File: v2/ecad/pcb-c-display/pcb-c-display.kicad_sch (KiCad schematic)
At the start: 126 parts, among them Q1 AO3401A P-FET high side, Q2 2N7002, Q3 2N7002, Q4 2N7002, U1 PCA9555PW 0x22: LEDs + switch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, U2 PCA9555PW 0x23: LEDs, bar, e-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, U5 USBLC6-2SC6 (2-line TVS), U6 USBLC6-2SC6 (2-line TVS), U7 USBLC6-2SC6 (2-line TVS), U8 USBLC6-2SC6 (2-line TVS)

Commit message: feat(release): A18 (dock holes 1.1 mm for the Preci-Dip 813 connector) and E3 (junction D-hole flat per the Amphenol 132170 drawing), C4 schematic with the switch part numbers, handoff rebuilt, A17 and E2 retired [MESHSAT-709]
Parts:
- SW_EMCON: value EMCON guarded latching toggle (closed = TX inhibit) -> EMCON guarded latching toggle (closed = TX inhibit); NKK M2012SD3A01, guard per ASSEMBLY.md section 9
- SW_LIGHT: value LIGHTING DAY/NIGHT/BLACKOUT toggle DPDT ON-ON-ON (pole 1: rail, pole 2: sense) -> LIGHTING DAY/NIGHT/BLACKOUT toggle DPDT ON-ON-ON (pole 1: rail, pole 2: sense); NKK M2044SD3A01 + AT401A boot
- SW_MAIN: value MAIN PWR 19 mm momentary, green ring (to X1202 external switch) -> MAIN PWR 19 mm momentary, green ring (to X1202 external switch); C&K ATP19-SL1-603-B0SA-03G
- SW_PI: value PI 16 mm recessed momentary, amber ring (to Pi 5 J2) -> PI 16 mm recessed momentary, amber ring (to Pi 5 J2); C&K ATP16-SL1-403-M0SA-04G (orange ring)
- SW_SOS: value SOS guarded momentary toggle (red cover) -> SOS guarded momentary toggle (red cover); NKK M2015SD3A01, guard per ASSEMBLY.md section 9
- SW_TEST: value TEST/ACK 16 mm momentary, white ring -> TEST/ACK 16 mm momentary, white ring; C&K ATP16-SL1-203-M0SA-04G
- SW_ZERO: value ZEROIZE guarded momentary toggle (hold 5 s) -> ZEROIZE guarded momentary toggle (hold 5 s); NKK M2015SD3A01, guard per ASSEMBLY.md section 9

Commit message: feat(ecad): PCB-C C5 finished, the sealed face (0 hard, 0 unrouted, 272 vias); die-cut seal outlines as DXF; case template with the seal parts named [MESHSAT-709]
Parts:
- removed J_X1202SW: lead to the X1202 external-switch pins (XH2.5), Connector_JST:JST_XH_B2B-XH-A_1x02_P2.50mm_Vertical, symbol Connector_Generic:Conn_01x02
- added J_MAINSW: MAIN button lead to PCB-A J_MAINSW (XH2.5 at the 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, meshsat:LeadLands_1x02, symbol Connector_Generic:Conn_01x02
- BZ1: value active piezo 5 V 85 dB -> IP67 panel-mount sounder, 5 V DC continuous, bezel gasket on the face, two flying leads (part per docs/respin-research-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; footprint Buzzer_Beeper:Buzzer_12x9.5RM7.6 -> meshsat:PanelSounder
- H1, H10, H11, H12, H13, H14, H15, H16, H2, H3, H4, H5, H6, H7, H8, H9: value frame screw M3, GND bond -> frame screw M3 x 10, GND bond through the bonded sealing washer on the underside land; footprint MountingHole:MountingHole_3.2mm_M3_Pad -> meshsat:FrameScrew_M3_GND
- J_EPD: value e-paper module lead: BUSY RES D/C CS SCL SDA GND VCC -> e-paper module lead: BUSY RES D/C CS SCL SDA GND VCC (SMD header on the underside); footprint Connector_PinHeader_2.54mm:PinHeader_1x08_P2.54mm_Vertical -> Connector_PinHeader_2.54mm:PinHeader_1x08_P2.54mm_Vertical_SMD_Pin1Left
- J_PANEL: footprint Connector_IDC:IDC-Header_2x10_P2.54mm_Vertical -> Connector_IDC:IDC-Header_2x10_P2.54mm_Vertical_SMD
- J_PIJ2: value lead to the Pi 5 J2 power-button pads (XH2.5) -> lead to the Pi 5 J2 power-button pins: two solder lands on the underside, soldered and beaded; footprint Connector_JST:JST_XH_B2B-XH-A_1x02_P2.50mm_Vertical -> meshsat:LeadLands_1x02
- SW_EMCON: value EMCON guarded latching toggle (closed = TX inhibit); NKK M2012SD3A01, guard per ASSEMBLY.md section 9 -> EMCON locking toggle (closed = TX inhibit; APEM 5636ADKB-2V, both positions locked; ruling 32.13); K front seal in the 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
- SW_LIGHT: value LIGHTING DAY/NIGHT/BLACKOUT toggle DPDT ON-ON-ON (pole 1: rail, pole 2: sense); NKK M2044SD3A01 + AT401A boot -> LIGHTING DAY/NIGHT/BLACKOUT toggle DPDT ON-ON-ON (pole 1: rail, pole 2: sense); NKK M2044SD3A01 on the D3 splashproof b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
- SW_MAIN: value MAIN PWR 19 mm momentary, green ring (to X1202 external switch); C&K ATP19-SL1-603-B0SA-03G -> MAIN PWR 19 mm momentary, green ring (to PCB-A J_MAINSW); C&K ATP19-SL1-603-B0SA-03G; silicone gasket washer under the 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
- SW_PI: value PI 16 mm recessed momentary, amber ring (to Pi 5 J2); C&K ATP16-SL1-403-M0SA-04G (orange ring) -> PI 16 mm recessed momentary, amber ring (to Pi 5 J2); C&K ATP16-SL1-403-M0SA-04G (orange ring); silicone gasket washer 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
- SW_SOS: value SOS guarded momentary toggle (red cover); NKK M2015SD3A01, guard per ASSEMBLY.md section 9 -> SOS locking toggle, maintained (APEM 5636ADKB-2V, both positions locked, red boot; ruling 32.13); K front seal in the k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
- SW_TEST: value TEST/ACK 16 mm momentary, white ring; C&K ATP16-SL1-203-M0SA-04G -> TEST/ACK 16 mm momentary, white ring; C&K ATP16-SL1-203-M0SA-04G; silicone gasket washer under the bezel
- SW_ZERO: value ZEROIZE guarded momentary toggle (hold 5 s); NKK M2015SD3A01, guard per ASSEMBLY.md section 9 -> ZEROIZE locking toggle, maintained (APEM 5636ADKB-2V, both positions locked; ruling 32.13); K front seal in the keyed 6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
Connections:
- net X1202SW_A renamed MAINSW_A
- net X1202SW_A2 renamed MAINSW_A2
- net MAINSW_A2: now also J_MAINSW.1 (Pin_1)
- net X1202SW_B renamed MAINSW_B
- net X1202SW_B2 renamed MAINSW_B2
- net MAINSW_B2: now also J_MAINSW.2 (Pin_2)

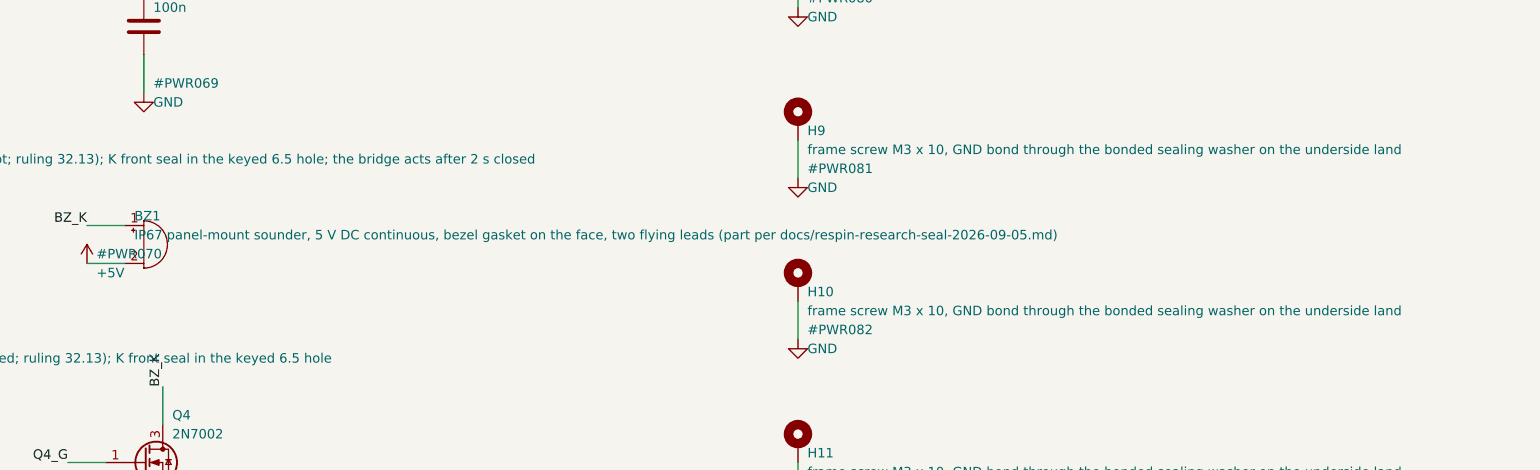
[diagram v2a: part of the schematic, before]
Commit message: docs: date correction, every event of section 32.10 onward is 4 September 2026 (headers carry the commit clock, research notes renamed); superseded board folders moved under boards/superseded [MESHSAT-709]
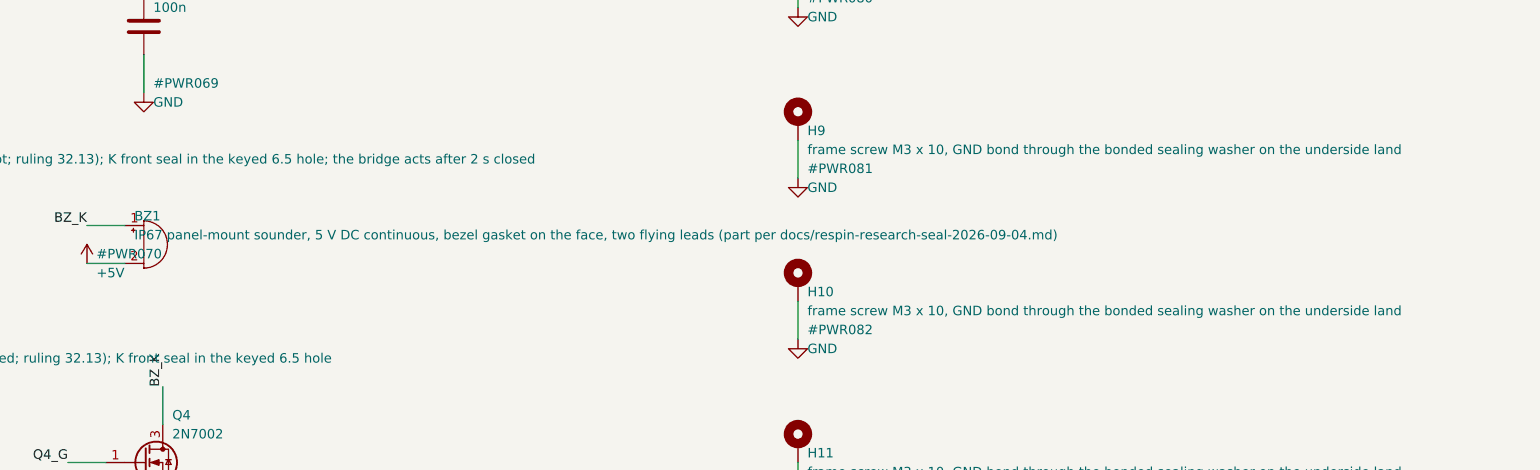
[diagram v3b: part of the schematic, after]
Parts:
- BZ1: value IP67 panel-mount sounder, 5 V DC continuous, bezel gasket on the face, two flying leads (part per docs/respin-research-seal-2026-09-05.md) -> IP67 panel-mount sounder, 5 V DC continuous, bezel gasket on the face, two flying leads (part per docs/respin-research-seal-2026-09-04.md)
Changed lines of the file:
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@@
 	(generator_version "9.0")
 	(paper "A1")
-	(title_block (title "MeshSat Field Kit carrier - PCB-C CONTROL PANEL") (date "2026-09-05") (rev "A") (company "MeshSat") (comment 1 "Phase C5 schematic (sealed face: no through-hole connector, panel-mount sounder, masked frame rings), generated by tools/gen_sch_c.py. Netlist style: every pin carries a stub and a net label.") (comment 2 "MESHSAT-709. FE1.1s hub on internal regulators; TPS2065C x2 + TPS22810 x4 switches (B4: LoRa and RockBLOCK channels at 2 A for the T-Beam 1W and 9704 bursts); INA219 per channel; PCA9555 EN/FAULT; both Pi UARTs to the RockBLOCK site via JP3/JP4."))
+	(title_block (title "MeshSat Field Kit carrier - PCB-C CONTROL PANEL") (date "2026-09-04") (rev "A") (company "MeshSat") (comment 1 "Phase C5 schematic (sealed face: no through-hole connector, panel-mount sounder, masked frame rings), generated by tools/gen_sch_c.py. Netlist style: every pin carries a stub and a net label.") (comment 2 "MESHSAT-709. FE1.1s hub on internal regulators; TPS2065C x2 + TPS22810 x4 switches (B4: LoRa and RockBLOCK channels at 2 A for the T-Beam 1W and 9704 bursts); INA219 per channel; PCA9555 EN/FAULT; both Pi UARTs to the RockBLOCK site via JP3/JP4."))
 	(text "RIBBON FROM PCB-B, RAILS, TVS, TEST POINTS" (exclude_from_sim no) (at 5.08 25.40 0) (effects (font (size 2.00 2.00) bold) (justify left bottom)))
 	(symbol (lib_id "Connector_Generic:Conn_02x10_Odd_Even") (at 39.37 53.34 0) (unit 1) (exclude_from_sim no) (in_bom yes) (on_board yes) (dnp no) (fields_autoplaced yes)
@@
 	(symbol (lib_id "Device:Buzzer") (at 656.59 234.95 0) (unit 1) (exclude_from_sim no) (in_bom yes) (on_board yes) (dnp no) (fields_autoplaced yes)
 		(property "Reference" "BZ1" (at 655.32 231.14 0) (effects (font (size 1.27 1.27)) (justify left)))
-		(property "Value" "IP67 panel-mount sounder, 5 V DC continuous, bezel gasket on the face, two flying leads (part per docs/respin-research-seal-2026-09-05.md)" (at 655.32 233.68 0) (effects (font (size 1.27 1.27)) (justify left)))
+		(property "Value" "IP67 panel-mount sounder, 5 V DC continuous, bezel gasket on the face, two flying leads (part per docs/respin-research-seal-2026-09-04.md)" (at 655.32 233.68 0) (effects (font (size 1.27 1.27)) (justify left)))
 		(property "Footprint" "meshsat:PanelSounder" (at 656.59 234.95 0) (effects (font (size 1.27 1.27)) (justify left) (hide yes)))
 		(property "Datasheet" "" (at 656.59 234.95 0) (effects (font (size 1.27 1.27)) (justify left) (hide yes)))

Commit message: feat(pcb-c): C6, the four-layer backer routed clean (0 hard, 0 open, 240 router vias); deliverable meshsat-pcb-c-revA-C6; order and review sets rebuilt with B15 and C6, B14 and C5 under superseded [MESHSAT-813]
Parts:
- removed H10, H11, H12, H13, H14, H15, H16, H7, H8, H9: frame screw M3 x 10, GND bond through the bonded 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, meshsat:FrameScrew_M3_GND, symbol Mechanical:MountingHole_Pad
- H1, H2, H3, H4, H5, H6: value frame screw M3 x 10, GND bond through the bonded sealing washer on the underside land -> M3 x 6 into the face plate's self-clinching standoff (C6 backer, 5 Sep 2026): GND bond to the plate; footprint meshsat:FrameScrew_M3_GND -> meshsat:BackerScrew_M3_GND
- SW_EMCON, SW_SOS, SW_ZERO: footprint meshsat:GuardedToggle_SPDT -> meshsat:ToggleBody_SPDT
- SW_LIGHT: footprint meshsat:PanelToggle_DPDT -> meshsat:ToggleBody_DPDT
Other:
- note added: "PLATE STANDOFF SCREWS, GND BOND"
- note removed: "FRAME SCREWS, GND BOND"

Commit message: feat(release): C7 (the panel backer ring) routed clean on the box, deliverable meshsat-pcb-c-revA-C7 [MESHSAT-830]
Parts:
- removed J_EPD: e-paper module lead: BUSY RES D/C CS SCL SDA GND 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, Connector_PinHeader_2.54mm:PinHeader_1x08_P2.54mm_Vertical_SMD_Pin1Left, symbol Connector_Generic:Conn_01x08
- removed J_PANEL: panel ribbon from PCB-B (IDC 2x10, underside), Connector_IDC:IDC-Header_2x10_P2.54mm_Vertical_SMD, symbol Connector_Generic:Conn_02x10_Odd_Even
- removed U5: USBLC6-2SC6 (2-line TVS), Package_TO_SOT_SMD:SOT-23-6, symbol Power_Protection:USBLC6-2SC6
- added C14, C15, C16: 1u, Capacitor_SMD:C_0603_1608Metric, symbol Device:C
- added C17, C18, C25, C26, C27, C29, C38: 100n, Capacitor_SMD:C_0603_1608Metric, symbol Device:C
- added C19, C20, C21, C22, C23, C24: 10n, Capacitor_SMD:C_0603_1608Metric, symbol Device:C
- added C28: 4.7u, Capacitor_SMD:C_0805_2012Metric, symbol Device:C
- added C30, C31, C32, C33, C34, C35, C36, C37: 1u 25V, Capacitor_SMD:C_0603_1608Metric, symbol Device:C
- added CAM_H1, CAM_H2: M2 screw of the USB camera module (25 x 25 board,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, MountingHole:MountingHole_2.2mm_M2, symbol Mechanical:MountingHole
- added D18: status (GPIO25), LED_SMD:LED_0603_1608Metric, symbol Device:LED
- added D19: SS2040FL: EPD_SW -> VGH, Diode_SMD:D_SOD-123F, symbol Device:D_Schottky
- added D20: SS2040FL: pump clamp, Diode_SMD:D_SOD-123F, symbol Device:D_Schottky
- added D21: SS2040FL: pump -> VGL, Diode_SMD:D_SOD-123F, symbol Device:D_Schottky
- added H7, H8: M3 x 6 into the face plate's self-clinching stand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, meshsat:BackerScrew_M3_GND, symbol Mechanical:MountingHole_Pad
- added J_EPD: Hirose FH34SRJ-24S-0.5SH ZIF for the E2370KS0C1 f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, meshsat:Hirose_FH34SRJ-24S, symbol Connector_Generic:EPD24
- added J_HSJ1: U-174/U headset jack 1 (Amphenol Nexus class, dra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, meshsat:PanelJack_17mm, symbol Mechanical:MountingHole
- added J_HSJ2: U-174/U headset jack 2 (Amphenol Nexus class, dra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, meshsat:PanelJack_17mm, symbol Mechanical:MountingHole
- added J_PANEL: panel ribbon from B16 J_PANEL (IDC 2x13 SMD, unde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, Connector_IDC:IDC-Header_2x13_P2.54mm_Vertical_SMD, symbol Connector_Generic:Conn_02x13_Odd_Even
- added L1: 10uH ATNR4010100MT 0.8 A (the boost inductor), Inductor_SMD:L_APV_ANR4020, symbol Device:L
- added Q5: AO3401A P-FET: the e-paper's supply switch (EPD_P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, Package_TO_SOT_SMD:SOT-23, symbol Transistor_FET:AO3401A
- added Q6: Si1308EDL class N-FET (RDS under 200 mOhm, VGS 2.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, Package_TO_SOT_SMD:SOT-23, symbol Transistor_FET:2N7002
- added R40: 300R, Resistor_SMD:R_0603_1608Metric, symbol Device:R
- added R41: 470R, Resistor_SMD:R_0603_1608Metric, symbol Device:R
- added R42: 10k, Resistor_SMD:R_0603_1608Metric, symbol Device:R
- added R43: 0.47R 1%, Resistor_SMD:R_0603_1608Metric, symbol Device:R
- added R44: 100R, Resistor_SMD:R_0603_1608Metric, symbol Device:R
- added R45: 100k, Resistor_SMD:R_0603_1608Metric, symbol Device:R
- added TP14: SPARE2, TestPoint:TestPoint_Pad_D1.5mm, symbol Connector:TestPoint
- added TP15: SPARE3, TestPoint:TestPoint_Pad_D1.5mm, symbol Connector:TestPoint
- added TP16: SPARE4, TestPoint:TestPoint_Pad_D1.5mm, symbol Connector:TestPoint
- added TP17: SPARE5, TestPoint:TestPoint_Pad_D1.5mm, symbol Connector:TestPoint
- added TP18: SPARE6, TestPoint:TestPoint_Pad_D1.5mm, symbol Connector:TestPoint
- added TP19: SPARE7, TestPoint:TestPoint_Pad_D1.5mm, symbol Connector:TestPoint
- added TP20: SPARE8, TestPoint:TestPoint_Pad_D1.5mm, symbol Connector:TestPoint
- added TP21: SPARE9, TestPoint:TestPoint_Pad_D1.5mm, symbol Connector:TestPoint
- added TP22: SPARE10, TestPoint:TestPoint_Pad_D1.5mm, symbol Connector:TestPoint
- added TP23: SPARE11, TestPoint:TestPoint_Pad_D1.5mm, symbol Connector:TestPoint
- added TP24: SPARE12, TestPoint:TestPoint_Pad_D1.5mm, symbol Connector:TestPoint
- added TP25: EPD_BUSY, TestPoint:TestPoint_Pad_D1.5mm, symbol Connector:TestPoint
- added TP26: EPD_VGH, TestPoint:TestPoint_Pad_D1.5mm, symbol Connector:TestPoint
- added TP27: EPD_VGL, TestPoint:TestPoint_Pad_D1.5mm, symbol Connector:TestPoint
- added TP28: HB1, TestPoint:TestPoint_Pad_D1.5mm, symbol Connector:TestPoint
- added TP29: HB2, TestPoint:TestPoint_Pad_D1.5mm, symbol Connector:TestPoint
- added TP30: HB3, TestPoint:TestPoint_Pad_D1.5mm, symbol Connector:TestPoint
- added TP31: SLOT_EN1, TestPoint:TestPoint_Pad_D1.5mm, symbol Connector:TestPoint
- added TP32: SLOT_EN2, TestPoint:TestPoint_Pad_D1.5mm, symbol Connector:TestPoint
- added TP33: SLOT_EN3, TestPoint:TestPoint_Pad_D1.5mm, symbol Connector:TestPoint
- added TP34: HDMI_SEL1, TestPoint:TestPoint_Pad_D1.5mm, symbol Connector:TestPoint
- added TP35: HDMI_SEL2, TestPoint:TestPoint_Pad_D1.5mm, symbol Connector:TestPoint
- added TP36: PI_SHDN_REQ, TestPoint:TestPoint_Pad_D1.5mm, symbol Connector:TestPoint
- added TP37: PI_KILL, TestPoint:TestPoint_Pad_D1.5mm, symbol Connector:TestPoint
- added TP38: SHORE_INHIBIT, TestPoint:TestPoint_Pad_D1.5mm, symbol Connector:TestPoint
- added TP39: PIJ2_A, TestPoint:TestPoint_Pad_D1.5mm, symbol Connector:TestPoint
- added TP40: PIJ2_B, TestPoint:TestPoint_Pad_D1.5mm, symbol Connector:TestPoint
- added U3: RP2040 panel controller (USB device on B16's slot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, Package_DFN_QFN:QFN-56-1EP_7x7mm_P0.4mm_EP3.2x3.2mm, symbol Connector_Generic:RP2040
- added U4: W25Q16JVUXIQ 16 Mbit QSPI flash (USON-8: 1 CS 2 D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, Package_SON:Winbond_USON-8-1EP_3x2mm_P0.5mm_EP0.2x1.6mm, symbol Connector_Generic:Conn_01x09
- added U5: TLV75533PDBV 3.3 V 500 mA LDO for the controller,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, Package_TO_SOT_SMD:SOT-23-5, symbol Connector_Generic:Conn_01x05
- added U9: 74LVC1G04 inverter (2 A 4 Y): EMCON_HW = NOT TX_I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, Package_TO_SOT_SMD:SOT-23-5, symbol Connector_Generic:Conn_01x05
- added U_LIGHT: Vishay VEML7700 ambient light sensor (1 SCL 2 VDD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, meshsat:Vishay_VEML7700, symbol Connector_Generic:Conn_01x04
- added Y1: 12 MHz ABM8-272-T3 (3225): 1 XIN, 3 XOUT, 2 and 4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, Crystal:Crystal_SMD_3225-4Pin_3.2x2.5mm, symbol Device:Crystal_GND24
- BZ1: value IP67 panel-mount sounder, 5 V DC continuous, bezel gasket on the face, two flying leads (part per docs/respin-research-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 -> IP67 panel-mount sounder, 5 V DC continuous, bezel gasket on the face, two flying leads (Floyd Bell MC-09-530-Q class)
- C10, C7, C8, C9: value 10n -> 100n; LCSC C57112 -> (none)
- C11, C12, C13: LCSC C14663 -> (none)
- C3, C4: value 100n -> 1u; LCSC C14663 -> (none)
- C5, C6: value 10n -> 15p NP0; footprint Capacitor_SMD:C_0603_1608Metric -> Capacitor_SMD:C_0402_1005Metric; LCSC C57112 -> (none)
- H1, H2, H3, H4, H5, H6: value M3 x 6 into the face plate's self-clinching standoff (C6 backer, 5 Sep 2026): GND bond to the plate -> M3 x 6 into the face plate's self-clinching standoff: GND bond to the plate
- JP1: value PANEL_ID strap (closed = variant B) -> BOOTSEL: short while powering to enter the USB bootloader
- JP2: value EPD RES from BCM7 instead of U2 (close to use) -> PANEL_ID strap (closed = variant B)
- J_MAINSW: value MAIN button lead to PCB-A J_MAINSW (XH2.5 at the PCB-A end): two solder lands on the underside, soldered and beaded -> MAIN button lead to A22 J_MAINSW (XH2.5 at the A22 end): two solder lands on the underside, soldered and beaded
- J_PIJ2: value lead to the Pi 5 J2 power-button pins: two solder lands on the underside, soldered and beaded -> PI button lead: two solder lands on the underside (the controller reads it as the module shutdown request)
- R1: value 10k -> 1k; LCSC C25804 -> (none)
- R10: value 47R -> 10k; LCSC C25118 -> C25804
- R11: value 100R -> 10k; LCSC C22775 -> C25804
- R12: value 100k -> 10k; LCSC C25803 -> C25804
- R13, R15: value 300R -> 10k; LCSC C23025 -> C25804
- R14: value 300R -> 100k; LCSC C23025 -> C25803
- R16: value 180R -> 10k; LCSC C25270 -> C25804
- R17: value 180R -> 2.2k; LCSC C25270 -> C4190
- R18: value 180R -> 47R; LCSC C25270 -> C25118
- R19: value 180R -> 100R; LCSC C25270 -> C22775
- R2, R3: value 10k -> 27R; LCSC C25804 -> (none)
- R20: value 180R -> 100k; LCSC C25270 -> C25803
- R21, R22: value 180R -> 300R; LCSC C25270 -> C23025
- R28, R32: value 300R -> 180R; LCSC C23025 -> C25270
- R29: value 1k -> 180R; LCSC C11702 -> C25270
- R30: value 100k -> 180R; LCSC C25803 -> C25270
- R31: value 470R -> 300R; LCSC C23179 -> C23025
- R33: value 470R -> 180R; LCSC C23179 -> C25270
- R34, R35: value 100R -> 180R; LCSC C22775 -> C25270
- R36: value 100R -> 300R; LCSC C22775 -> C23025
- R37: value 100R -> 1k; LCSC C22775 -> C11702
- R38: value 100R -> 100k; LCSC C22775 -> C25803
- R39: value 100k -> 470R; LCSC C25803 -> C23179
- R4: LCSC C25804 -> (none)
- R5: value 10k -> 1k (BOOTSEL); LCSC C25804 -> (none)
- R6: value 100k -> 1k; LCSC C25803 -> (none)
- R7, R8: value 10k -> 2.2k; LCSC C25804 -> (none)
- R9: value 2.2k -> 10k; LCSC C4190 -> C25804
- SW_EMCON: value EMCON locking toggle (closed = TX inhibit; APEM 5636ADKB-2V, both positions locked; ruling 32.13); K front seal in the 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 -> EMCON locking toggle (closed = TX inhibit, a hardware line: TX_INHIBIT_n low and EMCON_HW high; APEM 5636ADKB-2V, hinge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
- SW_MAIN: value MAIN PWR 19 mm momentary, green ring (to PCB-A J_MAINSW); C&K ATP19-SL1-603-B0SA-03G; silicone gasket washer under the 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 -> MAIN PWR 19 mm momentary, green ring (to A22 J_MAINSW); C&K ATP19-SL1-603-B0SA-03G; silicone gasket washer under the be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
- SW_PI: value PI 16 mm recessed momentary, amber ring (to Pi 5 J2); C&K ATP16-SL1-403-M0SA-04G (orange ring); silicone gasket washer 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 -> PI 16 mm recessed momentary, amber ring (PI_SHDN_REQ to the modules through the controller); C&K ATP16-SL1-403-M0SA-04G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
- SW_SOS: value SOS locking toggle, maintained (APEM 5636ADKB-2V, both positions locked, red boot; ruling 32.13); K front seal in the k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 -> SOS locking toggle, maintained (APEM 5636ADKB-2V, both positions locked, red boot, hinged safety cover per 32.50; rulin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
- SW_ZERO: value ZEROIZE locking toggle, maintained (APEM 5636ADKB-2V, both positions locked; ruling 32.13); K front seal in the keyed 6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 -> ZEROIZE locking toggle, maintained (APEM 5636ADKB-2V, hinged safety cover; ruling 32.13); K front seal in the keyed 6.5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
- TP1: value LED_RAIL -> SWCLK
- TP10: value SPARE3 -> TX_INHIBIT_n
- TP11: value SPARE4 -> EMCON_HW
- TP12: value SPARE5 -> ZEROIZE_HW
- TP13: value EPD_BUSY -> SPARE1
- TP2: value LED_RAIL_SW -> SWDIO
- TP3: value +5V -> C_RUN
- TP4: value +3V3 -> LED_RAIL
- TP5: value GND -> LED_RAIL_SW
- TP6: value EXP_INT -> +5V
- TP7: value TX_INHIBIT_n -> +3V3
- TP8: value SPARE1 -> GND
- TP9: value SPARE2 -> EXP_INT
- U1: value PCA9555PW 0x22: LEDs + switches -> PCA9555PW 0x22: LED sinks, light mode inputs
- U2: value PCA9555PW 0x23: LEDs, bar, e-paper control -> PCA9555PW 0x23: LED sinks, the battery bar, lamp test
- U6, U7, U8: value USBLC6-2SC6 (2-line TVS) -> USBLC6-2SC6
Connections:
- net EPD_CS_F is gone; now on net TX_A: R36.2
- net EPD_DC_F is gone; now on net Q3_G: R37.2
- net EPD_RES_ALT is gone; now on net PANEL_ID: JP2.1 (A)
- net EPD_SCL_F is gone; now on net BAT4_A: R34.2
- net EPD_SDA_F is gone; now on net BAT5_A: R35.2
- net SPI_MOSI is gone; now on net LED_RAIL: R35.1
- net SPI_SCLK is gone; now on net LED_RAIL: R34.1
- net +3V3: now also C10.1, C11.1, C12.1, C7.1, C8.1, C9.1, R10.2, R11.2, R12.2, R13.2, R14.2, R16.2, R7.2, R9.2, TP7.1, C16.1, C17.1, C18.1, C25.1, C38.1, Q5.2 (S), R42.2, U3.1 (IOVDD), U3.10 (IOVDD), U3.22 (IOVDD), U3.33 (IOVDD), U3.42 (IOVDD), U3.43 (ADC_AVDD), U3.44 (VREG_VIN), U3.48 (USB_VDD), U3.49 (IOVDD), U4.8 (Pin_8), U5.5 (Pin_5), U9.5 (Pin_5), U_LIGHT.2 (Pin_2); no longer C3.1, R1.2, R2.2, R3.2, R5.2, R6.2, TP4.1
- net +5V: now also C3.1, TP6.1, J_PANEL.1 (Pin_1), J_PANEL.2 (Pin_2), U5.1 (Pin_1), U5.3 (Pin_3); no longer TP3.1
- net BAT1_A: now also R31.2; no longer R23.2
- net BAT2_A: now also R32.2; no longer R24.2
- net BAT3_A: now also R33.2; no longer R25.2
- net BAT4_A: no longer R26.2
- net BAT5_A: no longer R27.2
- net CHG_A: now also R29.2; no longer R21.2
- net EPD_BUSY: now also J_EPD.9 (BUSY_N), TP25.1, U3.9 (GPIO7); no longer TP13.1, U2.15 (IO1_2)
- net EPD_DC: now also J_EPD.11 (DC), U3.6 (GPIO4); no longer R37.1, U6.3 (I/O2), U6.4 (I/O2)
- net EXP_INT: now also TP9.1, U8.3 (I/O2), U8.4 (I/O2), J_PANEL.6 (Pin_6), U3.36 (GPIO24); no longer TP6.1
- net GND: now also C11.2, C12.2, JP2.2 (B), R20.2, R38.2, TP8.1, C14.2, C15.2, C16.2, C17.2, C18.2, C19.2, C20.2, C21.2, C22.2, C23.2, C24.2, C25.2, C28.2, C29.2, C30.2, C32.2, C33.2, C34.2, C35.2, C36.2, C37.2, C38.2, D18.1 (K), D20.2 (A), H7.1, H8.1, J_EPD.17 (VSS), J_EPD.25 (SHIELD), J_EPD.26 (SHIELD), J_EPD.8 (BS), J_PANEL.14 (Pin_14), J_PANEL.17 (Pin_17), J_PANEL.3 (Pin_3), J_PANEL.9 (Pin_9), R43.2, R45.2, U3.19 (TESTEN), U3.57 (GND), U4.4 (Pin_4), U4.9 (Pin_9), U5.2 (Pin_2), U9.3 (Pin_3), U_LIGHT.3 (Pin_3), Y1.2 (G), Y1.4 (G); no longer R12.2, R30.2, R39.2, TP5.1
- net GPS_A: now also R27.2; no longer R19.2
- net LED_RAIL: now also R29.1, R30.1, R31.1, R36.1, TP4.1, R40.1, R41.1; no longer R13.1, R14.1, R15.1, R16.1, R17.1, R18.1, R19.1, R20.1, TP1.1
- net LED_RAIL_SW: now also R15.1, R17.1, R39.1, TP5.1; no longer R31.1, R7.1, R9.1, TP2.1
- net LIGHT_DAY_n: now also R12.1, U1.13 (IO1_0), C22.1; no longer C8.1, R4.1, U1.17 (IO1_4)
- net LIGHT_NIGHT_n: now also R13.1, U1.14 (IO1_1), C23.1; no longer C9.1, R5.1, U1.18 (IO1_5)
- net LTE_A: now also R26.2; no longer R18.2
- net MAINRING_A: now also R39.2; no longer R31.2
- net MAINSW_A2: now also C26.1; no longer C11.1
- net MAINSW_B2: now also C26.2; no longer C11.2
- net MCAUT_A: now also R22.2; no longer R14.2
- net MESH_A: now also R25.2; no longer R17.2
- net MSG_A: now also R30.2; no longer R22.2
- net MWARN_A: now also R21.2; no longer R13.2
- net PANEL_ID: now also R16.1, U1.15 (IO1_2); no longer JP1.1 (A), R8.1, U1.20 (IO1_7)
- net PANEL_PWM: now also R19.1, U3.11 (GPIO8); no longer R11.1, U8.1 (I/O1), U8.6 (I/O1)
- net PIJ2_A: now also TP39.1
- net PIJ2_A2: now also C27.1; no longer C12.1
- net PIJ2_B: now also TP40.1
- net PIJ2_B2: now also C27.2; no longer C12.2
- net PIRING_A: now also R40.2; no longer R32.2
- net PWM1: now also R44.1, U3.12 (GPIO9); no longer R38.1, U8.3 (I/O2), U8.4 (I/O2)
- net Q1_G: now also R17.2, R18.1; no longer R10.1, R9.2
- net Q2_D: now also R18.2; no longer R10.2
- net Q2_G: now also R19.2, R20.1; no longer R11.2, R12.1
- net Q3_G: now also R38.1; no longer R29.2, R30.1
- net Q4_G: now also R44.2, R45.1; no longer R38.2, R39.1
- net RAIL_SENSE: now also R15.2, U3.38 (GPIO26_A0); no longer R7.2, U1.19 (IO1_6)
- net SAT_A: now also R24.2; no longer R16.2
- net SCL: now also R8.1, J_PANEL.5 (Pin_5), U3.3 (GPIO1), U_LIGHT.1 (Pin_1)
- net SDA: now also R7.1, J_PANEL.4 (Pin_4), U3.2 (GPIO0), U_LIGHT.4 (Pin_4)
- net SHORE_A: now also R28.2; no longer R20.2
- net SOSACT_A: now also R23.2; no longer R15.2
- net SOS_SW: now also R9.1, C19.1, U3.40 (GPIO28_A2); no longer C5.1, R1.1, U1.13 (IO1_0)
- net SPARE1: now also TP13.1, U1.16 (IO1_3); no longer TP8.1, U2.16 (IO1_3)
- net SPARE2: now also U1.17 (IO1_4), TP14.1; no longer TP9.1, U2.17 (IO1_4)
- net SPARE3: now also U1.18 (IO1_5), TP15.1; no longer TP10.1, U2.18 (IO1_5)
- net SPARE4: now also U1.19 (IO1_6), TP16.1; no longer TP11.1, U2.19 (IO1_6)
- net SPARE5: now also U1.20 (IO1_7), TP17.1; no longer TP12.1, U2.20 (IO1_7)
- net TESTRING_A: now also R41.2; no longer R33.2
- net TEST_SW: now also R11.1, C21.1, U3.39 (GPIO27_A1); no longer C7.1, R3.1, U1.16 (IO1_3)
- net TR_APRS: now also R37.1, U8.1 (I/O1), U8.6 (I/O1), J_PANEL.7 (Pin_7), U3.35 (GPIO23); no longer R29.1
- net TX_A: no longer R28.2
- net TX_INHIBIT_n: now also R14.1, TP10.1, C24.1, J_PANEL.11 (Pin_11), U9.2 (Pin_2); no longer C10.1, R6.1, TP7.1, U1.14 (IO1_1)
- net EPD_RES renamed SPARE6
- net SPARE6: now also TP18.1; no longer JP2.2 (B)
- net SPI_CE0 renamed USB_PNL_P
- net USB_PNL_P: now also R2.2, J_PANEL.15 (Pin_15); no longer R36.1
- removed net ZEROIZE_SW: C6.1, R2.1, SW_ZERO.1 (Pin_1), U1.15 (IO1_2)
- new net BOOT_J: JP1.1 (A), R5.2
- new net C_DVDD: C14.1, C15.1, U3.23 (DVDD), U3.45 (VREG_VOUT), U3.50 (DVDD)
- new net C_RUN: R4.1, TP3.1, U3.26 (RUN)
- new net EMCON_HW: J_PANEL.8 (Pin_8), TP11.1, U3.32 (GPIO21), U9.4 (Pin_4)
- new net EPD_CS: J_EPD.12 (CSB), U3.7 (GPIO5)
- new net EPD_GDR: J_EPD.2 (GDR), Q6.1 (G)
- new net EPD_PUMP: C31.2, D20.1 (K), D21.2 (A)
- new net EPD_PWR_n: Q5.1 (G), R42.1, U3.41 (GPIO29_A3)
- new net EPD_RESE: J_EPD.3 (RESE), Q6.2 (S), R43.1
- new net EPD_RST: J_EPD.10 (RST_N), U3.8 (GPIO6)
- new net EPD_SCL: J_EPD.13 (SCL), U3.4 (GPIO2)
- new net EPD_SDA: J_EPD.14 (SDA), U3.5 (GPIO3)
- new net EPD_SW: C31.1, D19.1 (K), L1.2, Q6.3 (D)
- new net EPD_VCC: C28.1, C29.1, J_EPD.15 (VDDIO), J_EPD.16 (VDD), L1.1, Q5.3 (D)
- new net EPD_VCOM: C37.1, J_EPD.24 (VCOM)
- new net EPD_VDDD: C34.1, J_EPD.18 (VDDD)
- new net EPD_VDH: C35.1, J_EPD.20 (VDH)
- new net EPD_VDHR: C33.1, J_EPD.5 (VDHR)
- new net EPD_VDL: C36.1, J_EPD.22 (VDL)
- new net EPD_VGH: C30.1, D19.2 (A), J_EPD.21 (VGH), TP26.1
- new net EPD_VGL: C32.1, D21.1 (K), J_EPD.23 (VGL), TP27.1
- new net HB1: J_PANEL.18 (Pin_18), TP28.1, U3.13 (GPIO10)
- new net HB2: J_PANEL.19 (Pin_19), TP29.1, U3.14 (GPIO11)
- new net HB3: J_PANEL.20 (Pin_20), TP30.1, U3.15 (GPIO12)
- new net HDMI_SEL1: J_PANEL.12 (Pin_12), TP34.1, U3.27 (GPIO16)
- new net HDMI_SEL2: J_PANEL.13 (Pin_13), TP35.1, U3.28 (GPIO17)
- new net LED_STAT: R6.1, U3.37 (GPIO25)
- new net LED_STAT_A: D18.2 (A), R6.2
- new net PI_KILL: J_PANEL.25 (Pin_25), TP37.1, U3.30 (GPIO19)
- new net PI_SHDN_REQ: J_PANEL.24 (Pin_24), TP36.1, U3.29 (GPIO18)
- new net QSPI_D0: U3.53 (QSPI_SD0), U4.5 (Pin_5)
- new net QSPI_D1: U3.55 (QSPI_SD1), U4.2 (Pin_2)
- new net QSPI_D2: U3.54 (QSPI_SD2), U4.3 (Pin_3)
- new net QSPI_D3: U3.51 (QSPI_SD3), U4.7 (Pin_7)
- new net QSPI_SCLK: U3.52 (QSPI_SCLK), U4.6 (Pin_6)
- new net QSPI_SS: R5.1, U3.56 (QSPI_SS_N), U4.1 (Pin_1)
- new net SHORE_INHIBIT: J_PANEL.26 (Pin_26), TP38.1, U3.31 (GPIO20)
- new net SLOT_EN1: J_PANEL.21 (Pin_21), TP31.1, U3.16 (GPIO13)
- new net SLOT_EN2: J_PANEL.22 (Pin_22), TP32.1, U3.17 (GPIO14)
- new net SLOT_EN3: J_PANEL.23 (Pin_23), TP33.1, U3.18 (GPIO15)
- new net SPARE10: TP22.1, U2.18 (IO1_5)
- new net SPARE11: TP23.1, U2.19 (IO1_6)
- new net SPARE12: TP24.1, U2.20 (IO1_7)
- new net SPARE7: TP19.1, U2.15 (IO1_2)
- new net SPARE8: TP20.1, U2.16 (IO1_3)
- new net SPARE9: TP21.1, U2.17 (IO1_4)
- new net SWCLK: TP1.1, U3.24 (SWCLK)
- new net SWDIO: TP2.1, U3.25 (SWD)
- new net USB_DM_R: R3.1, U3.46 (USB_DM)
- new net USB_DP_R: R2.1, U3.47 (USB_DP)
- new net USB_PNL_N: J_PANEL.16 (Pin_16), R3.2, U6.3 (I/O2), U6.4 (I/O2)
- new net XIN: C5.1, U3.20 (XIN), Y1.1
- new net XOUT: C6.1, R1.2, Y1.3
- new net XOUT_R: R1.1, U3.21 (XOUT)
- new net ZEROIZE_HW: C20.1, J_PANEL.10 (Pin_10), R10.1, SW_ZERO.1 (Pin_1), TP12.1, U3.34 (GPIO22)
- no-connect marks 4 -> 11
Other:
- note added: "E-PAPER ZIF AND THE PDi BOOST, SOUNDER, LIGHT SENSOR, CAMERA MOUNT"
- note added: "EXPANDERS 0x22 / 0x23, MODE INPUTS, EMCON INVERTER, STRAPS"
- note added: "LED RAIL, INDICATORS, TX LAMP, SWITCHES AND LEADS"
- note added: "RIBBON FROM B16, 5 V, 3.3 V LDO, USB AND BUS ESD, FLAGS"
- note added: "RP2040 PANEL CONTROLLER, FLASH, CRYSTAL, BOOTSEL, BUS PULL-UPS"
- note added: "STANDOFF SCREWS (GND BOND), TEST POINTS, THE REST"
- note removed: "E-PAPER 3.7in LEAD + SOUNDER"
- note removed: "I2C EXPANDERS 0x22 / 0x23, SWITCH INPUTS, STRAPS"
- note removed: "INDICATORS (MIL-STD-1472 COLOUR CODE) + BATTERY BAR"
- note removed: "LED RAIL: LIGHTING TOGGLE, PWM HIGH-SIDE SWITCH"
- note removed: "PLATE STANDOFF SCREWS, GND BOND"
- note removed: "RIBBON FROM PCB-B, RAILS, TVS, TEST POINTS"
- note removed: "SWITCHES: MAIN PWR, PI, TEST/ACK, SOS, EMCON, ZEROIZE + POWER-BUTTON LEADS"
- note removed: "TX LAMP (HARDWARE FROM THE PTT MIRROR) + LAMP TEST"
- title: MeshSat Field Kit carrier - PCB-C CONTROL PANEL -> MeshSat Field Kit carrier - PCB-C CONTROL PANEL BACKER

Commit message: test(ecad): the golden schematic test, and the six board files regenerated to match their generators [MESHSAT-862]
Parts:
- D17: LCSC C2166 -> C7502705
- FB1, FB2, FB3, FB4: LCSC C1017 -> C1002
- R14: value 100k -> 10k; LCSC C25803 -> C25804
- R18: LCSC C25118 -> C23182
- R24, R25, R26, R27, R28, R29, R30, R32, R33, R34, R35: LCSC C25270 -> C22828
- R37: LCSC C11702 -> C21190
- SW_EMCON: value EMCON locking toggle (closed = TX inhibit, a hardware line: TX_INHIBIT_n low and EMCON_HW high; APEM 5636ADKB-2V, hinge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 -> EMCON locking toggle (closed = TX inhibit, a hardware line: TX_INHIBIT_n low and EMCON_HW low, the same sense; APEM 563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
- U1, U2: LCSC C50993 -> C2864778
- U3: value RP2040 panel controller (USB device on B16's slot-2 hub, the kit I2C master) -> RP2040 panel controller (USB device on B16's slot-1 hub, the kit I2C master)
- U9: value 74LVC1G04 inverter (2 A 4 Y): EMCON_HW = NOT TX_INHIBIT_n, the hardware emission-control line to every transmitter rail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 -> 74LVC1G34 non-inverting buffer (2 A 4 Y): EMCON_HW follows TX_INHIBIT_n; low = every transmitter inhibited (32.50 item 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
